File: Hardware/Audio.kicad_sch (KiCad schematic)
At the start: 6 parts, among them U9 PCM1809

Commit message: file renaming
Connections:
- net SPEECH: no longer names the net of U9.1 (IN1P)
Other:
- moved on the sheet: C36, C37, C38, C39, C40, U9

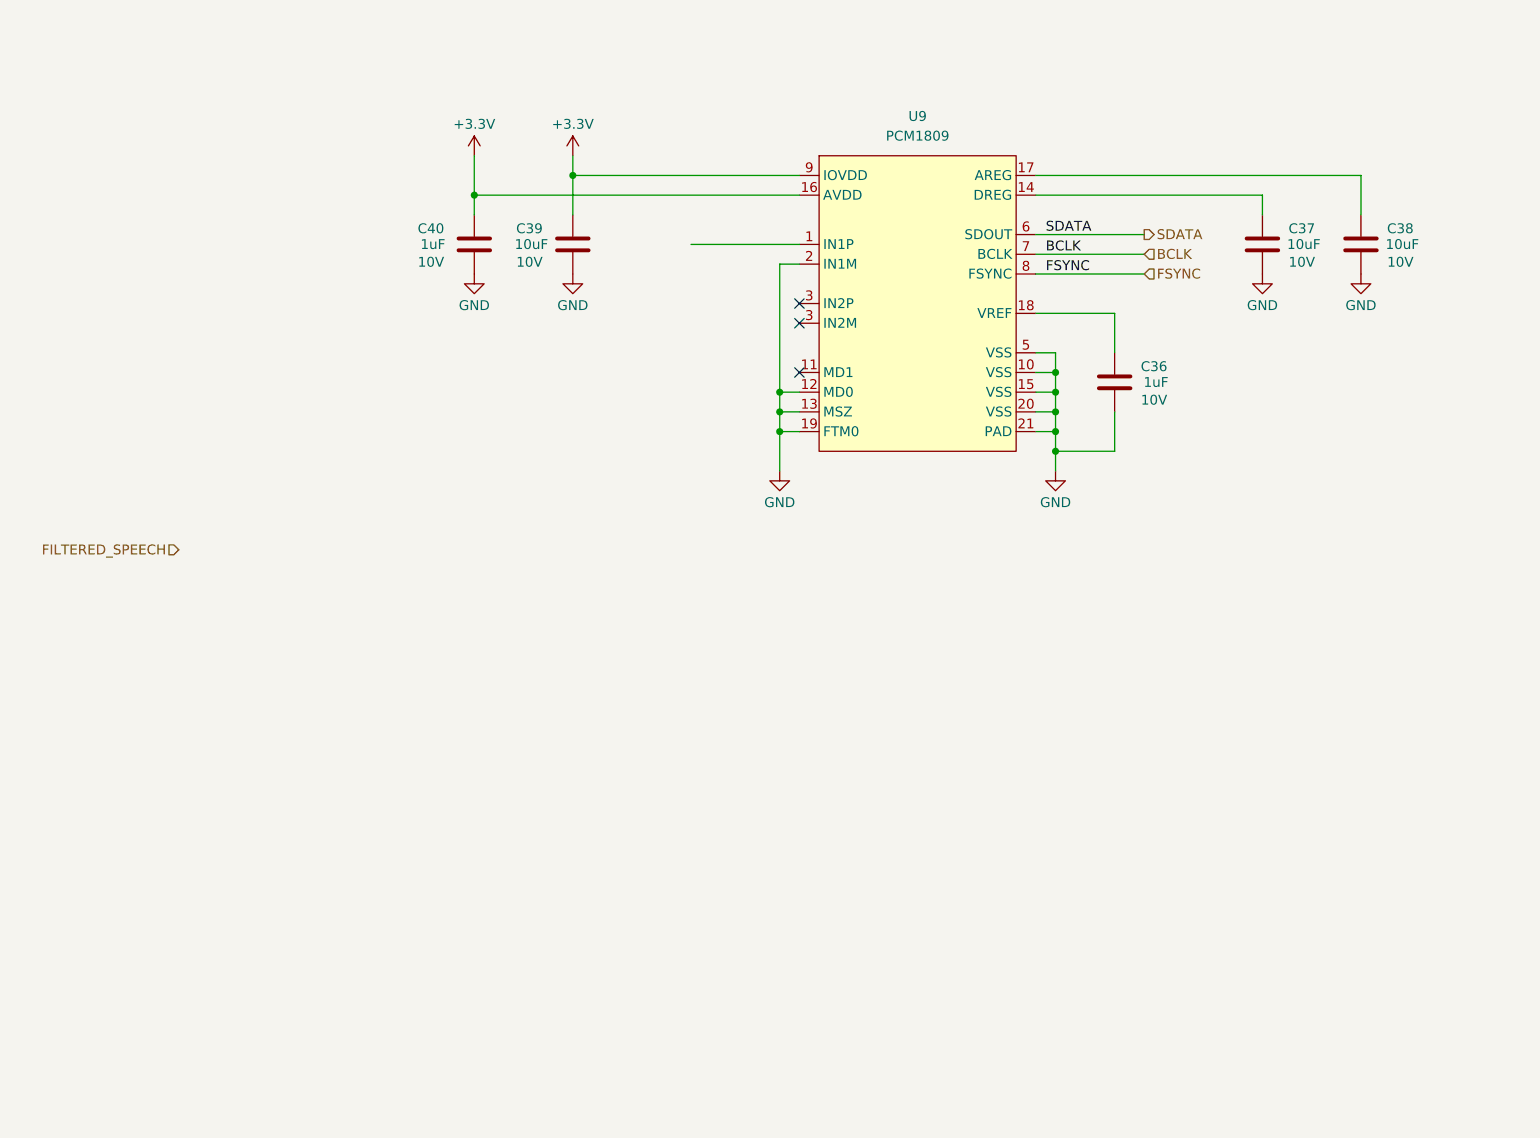
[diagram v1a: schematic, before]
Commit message: speaker output
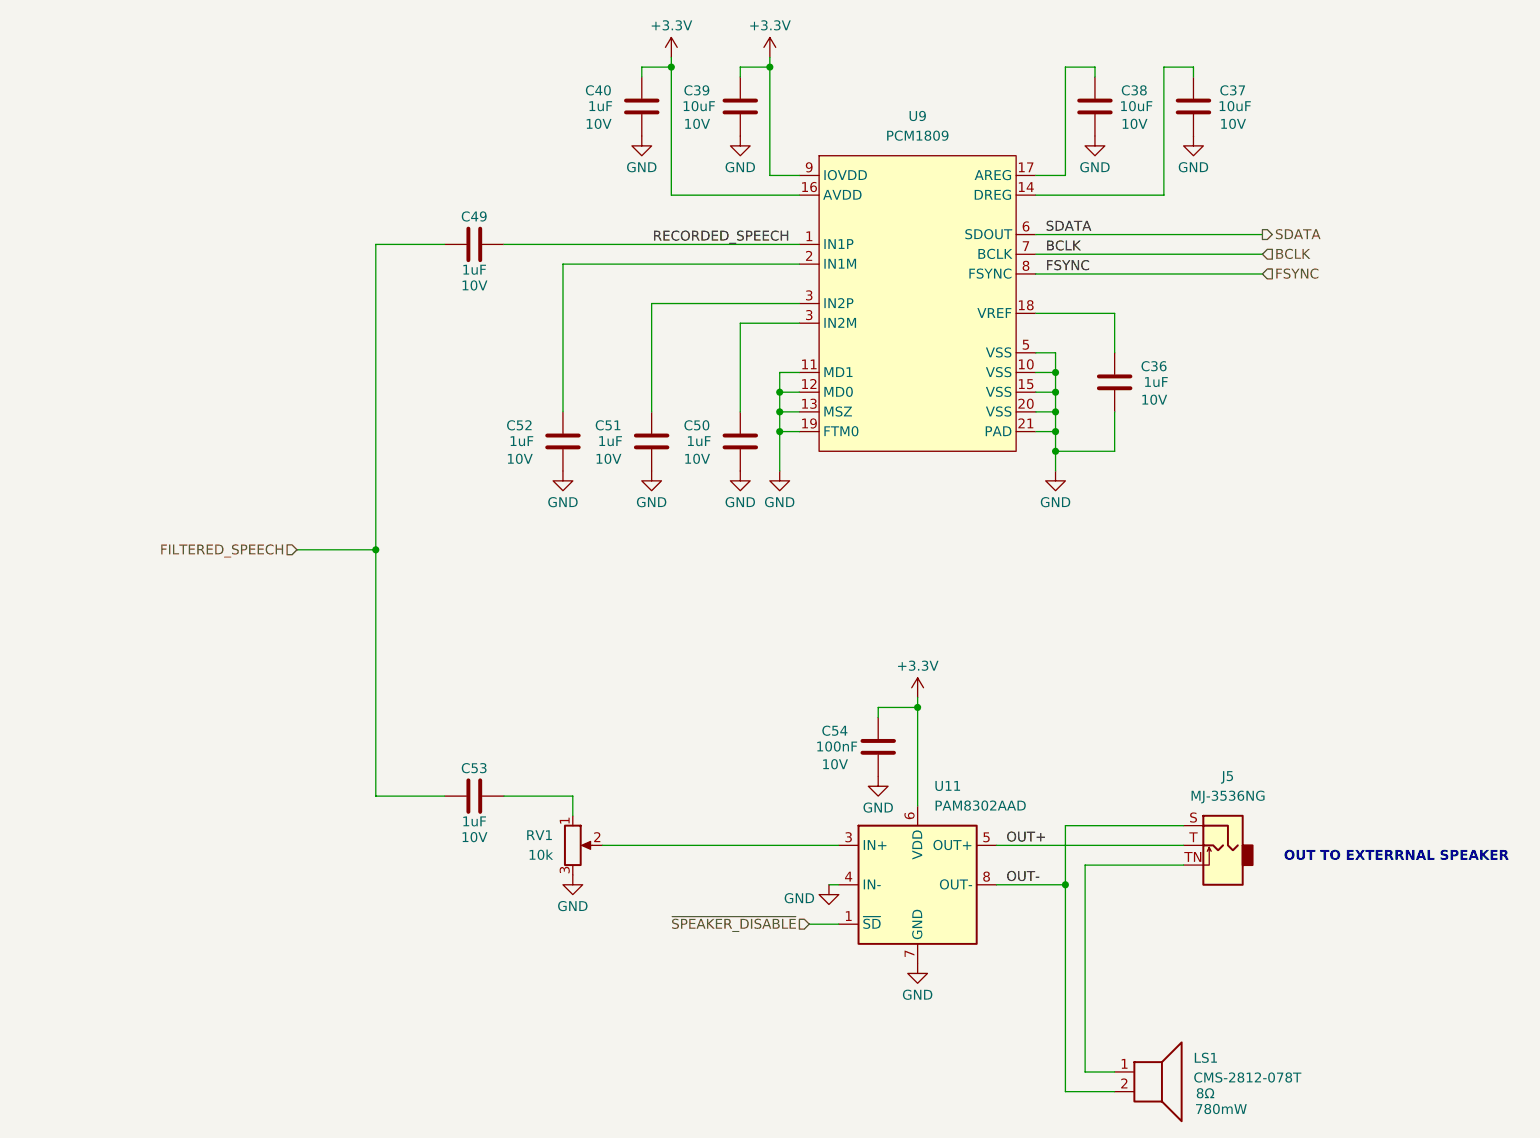
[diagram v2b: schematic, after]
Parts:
- added C49, C50, C51, C52, C53: 1uF, symbol Device:C
- added C54: 100nF, symbol Device:C
- added J5: MJ-3536NG, symbol Connector_Audio:AudioJack2_SwitchT
- added LS1: CMS-2812-078T, symbol Device:Speaker
- added RV1: 10k, symbol Device:R_Potentiometer
- added U11: PAM8302AAD, symbol Amplifier_Audio:PAM8302AAD
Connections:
- net +3.3V: now also C54.1, U11.6 (VDD)
- net FILTERED_SPEECH: now also C49.2, C53.2
- net GND: now also U9.11 (MD1), C50.2, C51.2, C52.2, C54.2, RV1.3, U11.4 (IN-), U11.7 (GND); no longer U9.2 (IN1M)
- net RECORDED_SPEECH: now reaches U9.1 (IN1P)
- net RECORDED_SPEECH: now also C49.1
- net at U9.3 (IN2M): now also C51.1
- new net: C50.1, U9.3 (IN2M)
- new net: J5.TN, LS1.1
- new net: C52.1, U9.2 (IN1M)
- new net: C53.1, RV1.1
- new net: RV1.2, U11.3 (IN+)
- new net OUT+: J5.T, U11.5 (OUT+)
- new net OUT-: J5.S, LS1.2, U11.8 (OUT-)
- new net ~{SPEAKER_DISABLE}: U11.1 (~{SD})
- no-connect marks 3 -> 0
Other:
- note added: "OUT TO EXTERRNAL SPEAKER"

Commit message: finalize audio outputs
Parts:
- removed J5: MJ-3536NG, symbol Connector_Audio:AudioJack2_SwitchT
- added C55: 1uF, symbol Device:C
- added J5: PJ-307C, symbol Connector_Audio:AudioJack3_SwitchTR
- added R34, R35: 100, symbol Device:R_US
- added R36: 100k, symbol Device:R_US
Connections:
- net FILTERED_SPEECH: now also C55.2
- net GND: now also J5.S, R36.2
- net OUT+: now also LS1.1
- new net: J5.R, R34.1
- new net: C55.1, R34.2, R35.2, R36.1
- new net: J5.T, R35.1
- no-connect marks 0 -> 2
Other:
- moved on the sheet: C53, C54, LS1, RV1, U11

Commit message: footprint assignment
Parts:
- C36, C40, C49, C50, C51, C52, C53, C55: footprint (none) -> Capacitor_SMD:C_0402_1005Metric; MPN (none) -> CL05A105KA5NQNC
- C37, C38, C39: footprint (none) -> Capacitor_SMD:C_0402_1005Metric; MPN (none) -> CL05A106MQ5NUNC
- C54: footprint (none) -> Capacitor_SMD:C_0402_1005Metric; MPN (none) -> GRM155R71A104KA01D
- J5: value PJ-307C -> SJ1-3535NG; footprint (none) -> Connector_Audio:Jack_3.5mm_CUI_SJ1-3535NG_Horizontal; MPN (none) -> SJ1-3535NG
- LS1: MPN (none) -> CMS-2812-078T
- U11: footprint (none) -> Package_SO:MSOP-8_3x3mm_P0.65mm; MPN (none) -> PAM8302AAD
- U9: footprint (none) -> Package_DFN_QFN:WQFN-20-1EP_3x3mm_P0.4mm_EP1.7x1.7mm; MPN (none) -> PCM1809

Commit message: link footprints to symbols
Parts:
- LS1: footprint (none) -> Digichiver:SPKR_CMS-2812-078T
- R34, R35: footprint (none) -> Resistor_SMD:R_0402_1005Metric; MPN (none) -> RC0402FR-07100RL
- R36: footprint (none) -> Resistor_SMD:R_0402_1005Metric; MPN (none) -> RC0402FR-07100KL
- RV1: footprint (none) -> Digichiver:PTV09; now left out of the parts list
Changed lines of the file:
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@@
 			)
 		)
-		(property "Footprint" ""
+		(property "Footprint" "Resistor_SMD:R_0402_1005Metric"
 			(at 234.696 130.556 90)
 			(hide yes)
@@
 			)
 		)
-		(property "Datasheet" ""
+		(property "Datasheet" "https://yageogroup.com/content/datasheet/asset/file/PYU-RC_GROUP_51_ROHS_L"
 			(at 234.95 129.54 0)
 			(hide yes)
@@
 		)
 		(property "KLC_S4.2_VREG_LX" ""
+			(at 234.95 129.54 90)
+			(hide yes)
+			(show_name no)
+			(do_not_autoplace no)
+			(effects
+				(font
+					(size 1.27 1.27)
+				)
+			)
+		)
+		(property "MPN" "RC0402FR-07100RL"
 			(at 234.95 129.54 90)
 			(hide yes)
@@
 			)
 		)
-		(property "Footprint" ""
+		(property "Footprint" "Resistor_SMD:R_0402_1005Metric"
 			(at 224.536 141.224 90)
 			(hide yes)
@@
 			)
 		)
-		(property "Datasheet" ""
+		(property "Datasheet" "https://yageogroup.com/content/datasheet/asset/file/PYU-RC_GROUP_51_ROHS_L"
 			(at 223.52 140.97 0)
 			(hide yes)
@@
 		)
 		(property "KLC_S4.2_VREG_LX" ""
+			(at 223.52 140.97 0)
+			(hide yes)
+			(show_name no)
+			(do_not_autoplace no)
+			(effects
+				(font
+					(size 1.27 1.27)
+				)
+			)
+		)
+		(property "MPN" "RC0402FR-07100KL"
 			(at 223.52 140.97 0)
 			(hide yes)
@@
 			)
 		)
-		(property "Footprint" ""
+		(property "Footprint" "Resistor_SMD:R_0402_1005Metric"
 			(at 234.696 135.636 90)
 			(hide yes)
@@
 			)
 		)
-		(property "Datasheet" ""
+		(property "Datasheet" "https://yageogroup.com/content/datasheet/asset/file/PYU-RC_GROUP_51_ROHS_L"
 			(at 234.95 134.62 0)
 			(hide yes)
@@
 		)
 		(property "KLC_S4.2_VREG_LX" ""
+			(at 234.95 134.62 90)
+			(hide yes)
+			(show_name no)
+			(do_not_autoplace no)
+			(effects
+				(font
+					(size 1.27 1.27)
+				)
+			)
+		)
+		(property "MPN" "RC0402FR-07100RL"
 			(at 234.95 134.62 90)
 			(hide yes)
@@
 		(body_style 1)
 		(exclude_from_sim no)
-		(in_bom yes)
+		(in_bom no)
 		(on_board yes)
 		(in_pos_files yes)
@@
 			)
 		)
-		(property "Footprint" ""
+		(property "Footprint" "Digichiver:PTV09"
 			(at 165.1 173.99 0)
 			(hide yes)
@@
 			)
 		)
-		(property "Footprint" ""
+		(property "Footprint" "Digichiver:SPKR_CMS-2812-078T"
 			(at 240.03 179.07 0)
 			(hide yes)

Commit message: layout complete
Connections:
- net at C50.1: now also U9.4 (IN2M); no longer U9.3 (IN2M)
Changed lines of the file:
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@@
 		(pin "1"
 		)
-		(pin "3"
+		(pin "4"
 		)
 		(pin "13"

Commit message: ac couple speaker amp input
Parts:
- added C56: 1uF, Capacitor_SMD:C_0402_1005Metric, symbol Device:C
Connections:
- net GND: now also C56.2; no longer U11.4 (IN-)
- new net: C56.1, U11.4 (IN-)
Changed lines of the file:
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@@
 	(wire
 		(pts
-			(xy 195.58 184.15) (xy 199.39 184.15)
+			(xy 190.5 184.15) (xy 199.39 184.15)
 		)
 		(stroke
@@
 		(pts
 			(xy 190.5 63.5) (xy 190.5 64.77)
+		)
+		(stroke
+			(width 0)
+			(type default)
+		)
+	)
+	(wire
+		(pts
+			(xy 198.12 179.07) (xy 198.12 186.69)
 		)
 		(stroke
@@
 	(hierarchical_label "~{SPEAKER_DISABLE}"
 		(shape input)
-		(at 195.58 184.15 180)
+		(at 190.5 184.15 180)
 		(effects
 			(font
@@
 	)
 	(symbol
-		(lib_id "power:GND")
-		(at 198.12 179.07 0)
-		(unit 1)
-		(body_style 1)
-		(exclude_from_sim no)
-		(in_bom yes)
-		(on_board yes)
-		(in_pos_files yes)
-		(dnp no)
-		(property "Reference" "#PWR0107"
-			(at 198.12 185.42 0)
-			(hide yes)
-			(show_name no)
-			(do_not_autoplace no)
-			(effects
-				(font
-					(size 1.27 1.27)
-				)
-			)
-		)
-		(property "Value" "GND"
-			(at 194.31 180.848 0)
-			(show_name no)
-			(do_not_autoplace no)
-			(effects
-				(font
-					(size 1.27 1.27)
-				)
-			)
-		)
-		(property "Footprint" ""
-			(at 198.12 179.07 0)
-			(hide yes)
-			(show_name no)
-			(do_not_autoplace no)
-			(effects
-				(font
-					(size 1.27 1.27)
-				)
-			)
-		)
-		(property "Datasheet" ""
-			(at 198.12 179.07 0)
-			(hide yes)
-			(show_name no)
-			(do_not_autoplace no)
-			(effects
-				(font
-					(size 1.27 1.27)
-				)
-			)
-		)
-		(property "Description" "Power symbol creates a global label with name \"GND\" , ground"
-			(at 198.12 179.07 0)
-			(hide yes)
-			(show_name no)
-			(do_not_autoplace no)
-			(effects
-				(font
-					(size 1.27 1.27)
-				)
-			)
-		)
-		(pin "1"
-		)
-		(instances
-			(project "Digichiver"
-				(path "/51de4045-d2a2-42d9-b145-319acd726bb6/d8e5fb35-4d7b-4489-a789-c25f01344ad2"
-					(reference "#PWR0107")
-					(unit 1)
-				)
-			)
-		)
-	)
-	(symbol
 		(lib_id "Device:C")
 		(at 186.69 113.03 0)
@@
 	(symbol
 		(lib_id "Device:C")
+		(at 198.12 190.5 0)
+		(unit 1)
+		(body_style 1)
+		(exclude_from_sim no)
+		(in_bom yes)
+		(on_board yes)
+		(in_pos_files yes)
+		(dnp no)
+		(property "Reference" "C56"
+			(at 192.532 188.468 0)
+			(show_name no)
+			(do_not_autoplace no)
+			(effects
+				(font
+					(size 1.27 1.27)
+				)
+			)
+		)
+		(property "Value" "1uF"
+			(at 192.786 190.5 0)
+			(show_name no)
+			(do_not_autoplace no)
+			(effects
+				(font
+					(size 1.27 1.27)
+				)
+			)
+		)
+		(property "Footprint" "Capacitor_SMD:C_0402_1005Metric"
+			(at 199.0852 194.31 0)
+			(hide yes)
+			(show_name no)
+			(do_not_autoplace no)
+			(effects
+				(font
+					(size 1.27 1.27)
+				)
+			)
+		)
+		(property "Datasheet" "https://mm.digikey.com/Volume0/opasdata/d220001/medias/docus/41/CL05A105KA5NQNC.pdf"
+			(at 198.12 190.5 0)
+			(hide yes)
+			(show_name no)
+			(do_not_autoplace no)
+			(effects
+				(font
+					(size 1.27 1.27)
+				)
+			)
+		)
+		(property "Description" "Unpolarized capacitor"
+			(at 198.12 190.5 0)
+			(hide yes)
+			(show_name no)
+			(do_not_autoplace no)
+			(effects
+				(font
+					(size 1.27 1.27)
+				)
+			)
+		)
+		(property "Voltage" "10V"
+			(at 192.532 192.786 0)
+			(show_name no)
+			(do_not_autoplace no)
+			(effects
+				(font
+					(size 1.27 1.27)
+				)
+			)
+		)
+		(property "MPN" "CL05A105KA5NQNC"
+			(at 198.12 190.5 0)
+			(hide yes)
+			(show_name no)
+			(do_not_autoplace no)
+			(effects
+				(font
+					(size 1.27 1.27)
+				)
+			)
+		)
+		(property "KLC_S4.2_DVDD" ""
+			(at 198.12 190.5 0)
+			(hide yes)
+			(show_name no)
+			(do_not_autoplace no)
+			(effects
+				(font
+					(size 1.27 1.27)
+				)
+			)
+		)
+		(property "KLC_S4.2_VREG_LX" ""
+			(at 198.12 190.5 0)
+			(hide yes)
+			(show_name no)
+			(do_not_autoplace no)
+			(effects
+				(font
+					(size 1.27 1.27)
+				)
+			)
+		)
+		(pin "2"
+		)
+		(pin "1"
+		)
+		(instances
+			(project "Digichiver"
+				(path "/51de4045-d2a2-42d9-b145-319acd726bb6/d8e5fb35-4d7b-4489-a789-c25f01344ad2"
+					(reference "C56")
+					(unit 1)
+				)
+			)
+		)
+	)
+	(symbol
+		(lib_id "Device:C")
 		(at 175.26 113.03 0)
 		(unit 1)
@@
 					(unit 1)
 				)
+			)
+		)
+	)
+	(symbol
+		(lib_id "power:GND")
+		(at 198.12 194.31 0)
+		(unit 1)
+		(body_style 1)
+		(exclude_from_sim no)
+		(in_bom yes)
+		(on_board yes)
+		(in_pos_files yes)
+		(dnp no)
+		(property "Reference" "#PWR0107"
+			(at 198.12 200.66 0)
+			(hide yes)
+			(show_name no)
+			(do_not_autoplace no)
+			(effects
+				(font
+					(size 1.27 1.27)
+				)
+			)
+		)
+		(property "Value" "GND"
+			(at 194.31 196.088 0)
+			(show_name no)
+			(do_not_autoplace no)
+			(effects
+				(font
+					(size 1.27 1.27)
+				)
+			)
+		)
+		(property "Footprint" ""
+			(at 198.12 194.31 0)
+			(hide yes)
+			(show_name no)
+			(do_not_autoplace no)
+			(effects
+				(font
+					(size 1.27 1.27)
+				)
+			)
+		)
+		(property "Datasheet" ""
+			(at 198.12 194.31 0)
+			(hide yes)
+			(show_name no)
+			(do_not_autoplace no)
+			(effects
+				(font
+					(size 1.27 1.27)
+				)
+			)
+		)
+		(property "Description" "Power symbol creates a global label with name \"GND\" , ground"
+			(at 198.12 194.31 0)
+			(hide yes)
+			(show_name no)
+			(do_not_autoplace no)
+			(effects
+				(font
+					(size 1.27 1.27)
+				)
+			)
+		)
+		(pin "1"
+		)
+		(instances
+			(project "Digichiver"
+				(path "/51de4045-d2a2-42d9-b145-319acd726bb6/d8e5fb35-4d7b-4489-a789-c25f01344ad2"
+					(reference "#PWR0107")
+					(unit 1)
+				)

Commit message: generate outputs
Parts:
- C36, C40, C49, C50, C51, C52, C53, C55, C56: JLCPCB Part # (none) -> C52923; Voltage 10V -> 25V
- C37, C38, C39: JLCPCB Part # (none) -> C315248; MPN CL05A106MQ5NUNC -> CL05A106MP5NUNC
- C54: JLCPCB Part # (none) -> C105883; MPN GRM155R71A104KA01D -> CC0402KRX7R8BB104; Voltage 10V -> 25V
- J5: JLCPCB Part # (none) -> C4991610
- R34, R35: JLCPCB Part # (none) -> C106232
- R36: JLCPCB Part # (none) -> C60491
- U11: JLCPCB Part # (none) -> C112137; MPN PAM8302AAD -> PAM8302AADCR
- U9: JLCPCB Part # (none) -> C38558044; MPN PCM1809 -> PCM1809IRTER
